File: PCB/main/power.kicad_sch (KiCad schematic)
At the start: 0 parts

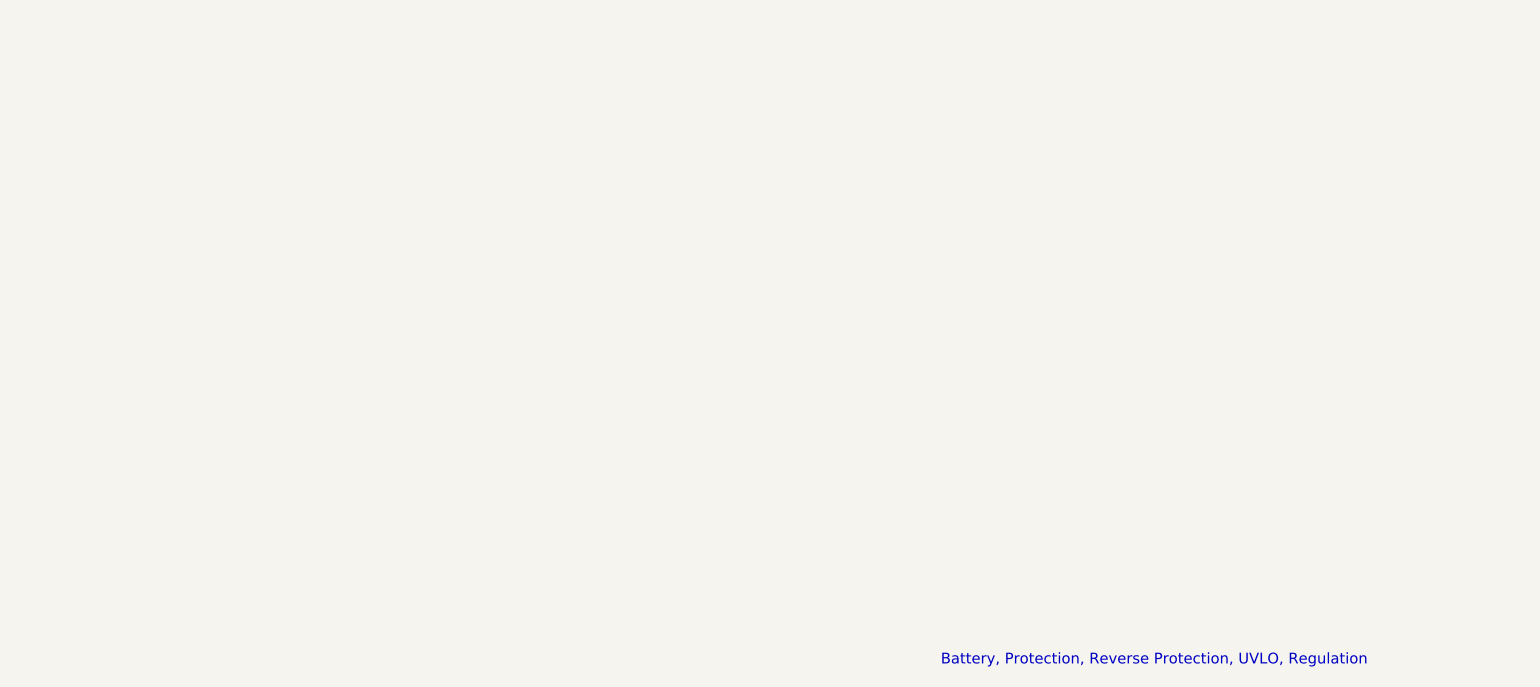
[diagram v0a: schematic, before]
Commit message: Added battery charger and polarity protection
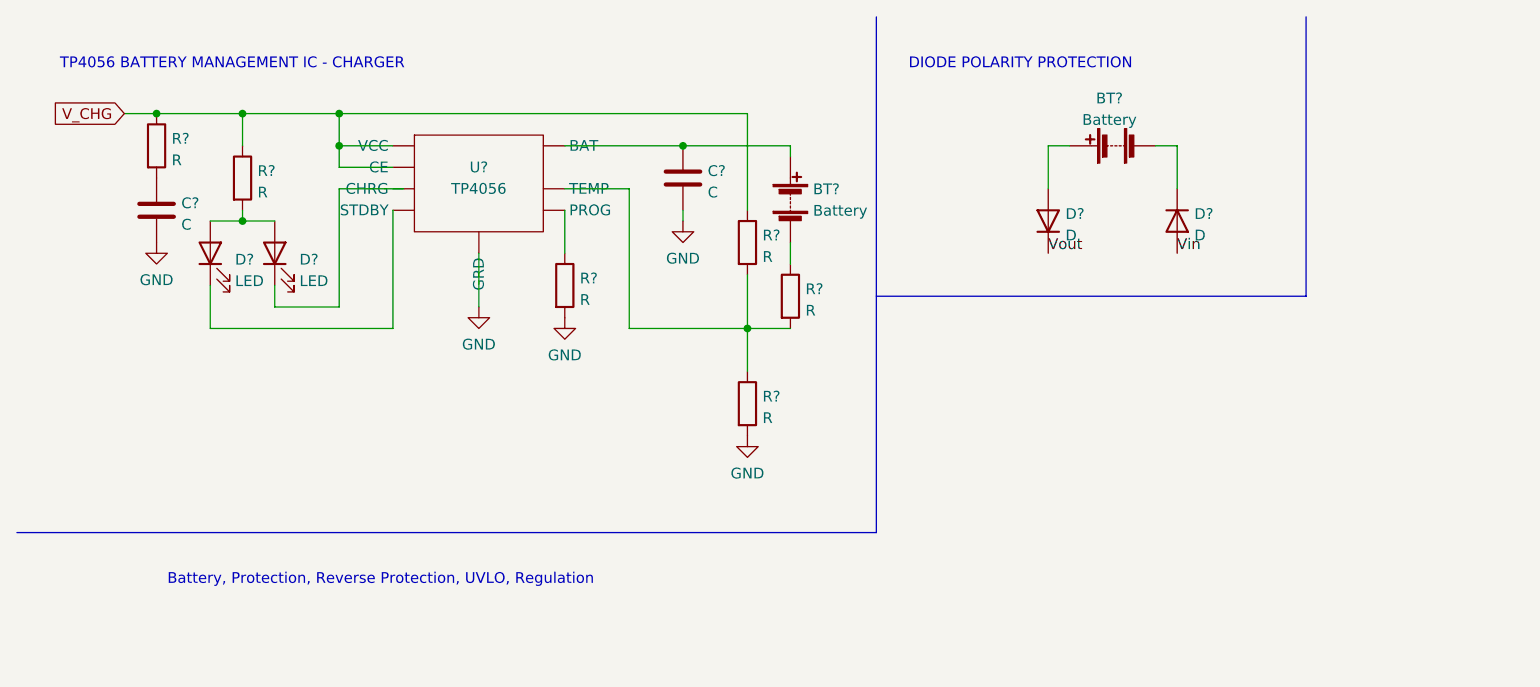
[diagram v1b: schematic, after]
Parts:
- added BT? (x2): Battery, symbol Device:Battery
- added C? (x2): C, symbol Device:C
- added D? (x2): D, symbol Device:D
- added D? (x2): LED, symbol Device:LED
- added R? (x6): R, symbol Device:R
- added U?: TP4056, symbol 000_MY_SYMBOLS:TP4056
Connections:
- new net: BT?.1 (+), C?.1
- new net: BT?.2 (-), R?.1
- new net: BT?.1 (+), D?.2 (A)
- new net: D?.2 (A), D?.2 (A), R?.2
- new net: BT?.2 (-), D?.1 (K)
- new net: C?.1, R?.2
- new net: R?.1, R?.2, R?.2
- new net GND: C?.2, C?.2, R?.2, R?.2
- new net V_CHG: R?.1, R?.1, R?.1
- new net Vin: D?.2 (A)
- new net Vout: D?.1 (K)
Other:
- note added: "DIODE POLARITY PROTECTION"
- note added: "TP4056 BATTERY MANAGEMENT IC - CHARGER"

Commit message: Added Added global V3.3 label & power BOM again again
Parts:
- removed BT?: Battery, symbol Device:Battery
- added C3: 0.47u, symbol Device:C
- added C4: 33u, symbol Device:C
- added D5: D_Zener, symbol Device:D_Zener
- added Q1: Q_PMOS_DGS, symbol Device:Q_PMOS_DGS
- added R10, R11, R12, R7, R8, R9: R, symbol Device:R
- added U2: LM3940, symbol 000_MY_SYMBOLS:LM3940
- added U3: OPAMP, symbol pspice:OPAMP
- gave numbers to parts that had none: 14
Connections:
- net GND: now also U1. (VCC), C3.2, C4.2, U2. (OUT)
- net V_CHG: now also U1. (VCC)
- net Vin: now also R10.2, R8.2, U3.5 (V-)
- net Vout: now also Q1.3 (S), R7.1, R9.1, U3.4 (V+)
- net CHG+: now reaches C2.1
- net CHG+: now also BT1.1 (+), D3.2 (A), U1. (VCC)
- net CHG-: now reaches R6.1
- net CHG-: now also BT1.2 (-), D4.1 (K)
- net at D1.1 (K): now also U1. (VCC)
- net at D2.1 (K): now also U1. (VCC)
- net at R4.2, R5.1, R6.2: now also U1. (VCC)
- net at R3.1: now also U1. (VCC)
- new net: R7.2, R8.1, U3.2 (-)
- new net: Q1.2 (G), R11.1
- new net: R11.2, R12.1, U3.3
- new net: D5.2 (A), R10.1, R12.2
- new net: D5.1 (K), R9.2, U3.1 (+)
- new net: C3.1, U2. (OUT)
- new net OUTPUT VOLTAGE: Q1.1 (D)
- new net V3.3: C4.1, U2. (OUT)
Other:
- note added: "ALL VALUES TBC"
- note added: "Cameron made this."
- note added: "UNDER VOLTAGE LOCKOUT"
- note added: "VOLTAGE REGULATOR"
- moved on the sheet: D3

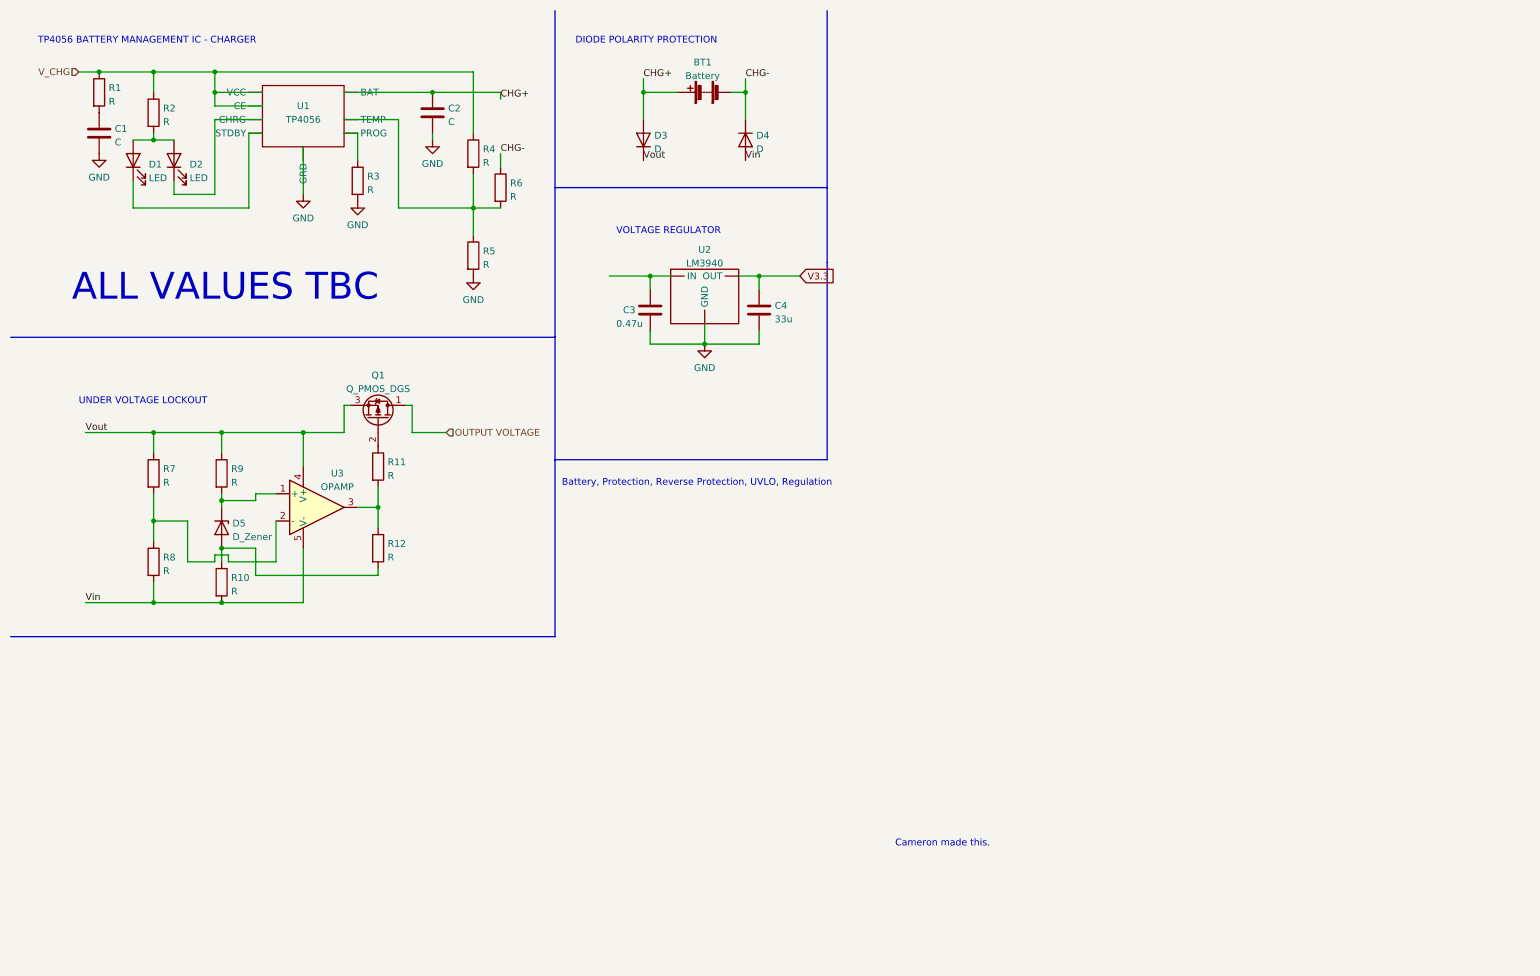
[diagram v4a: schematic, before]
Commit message: Updated power subsystem to V0.3
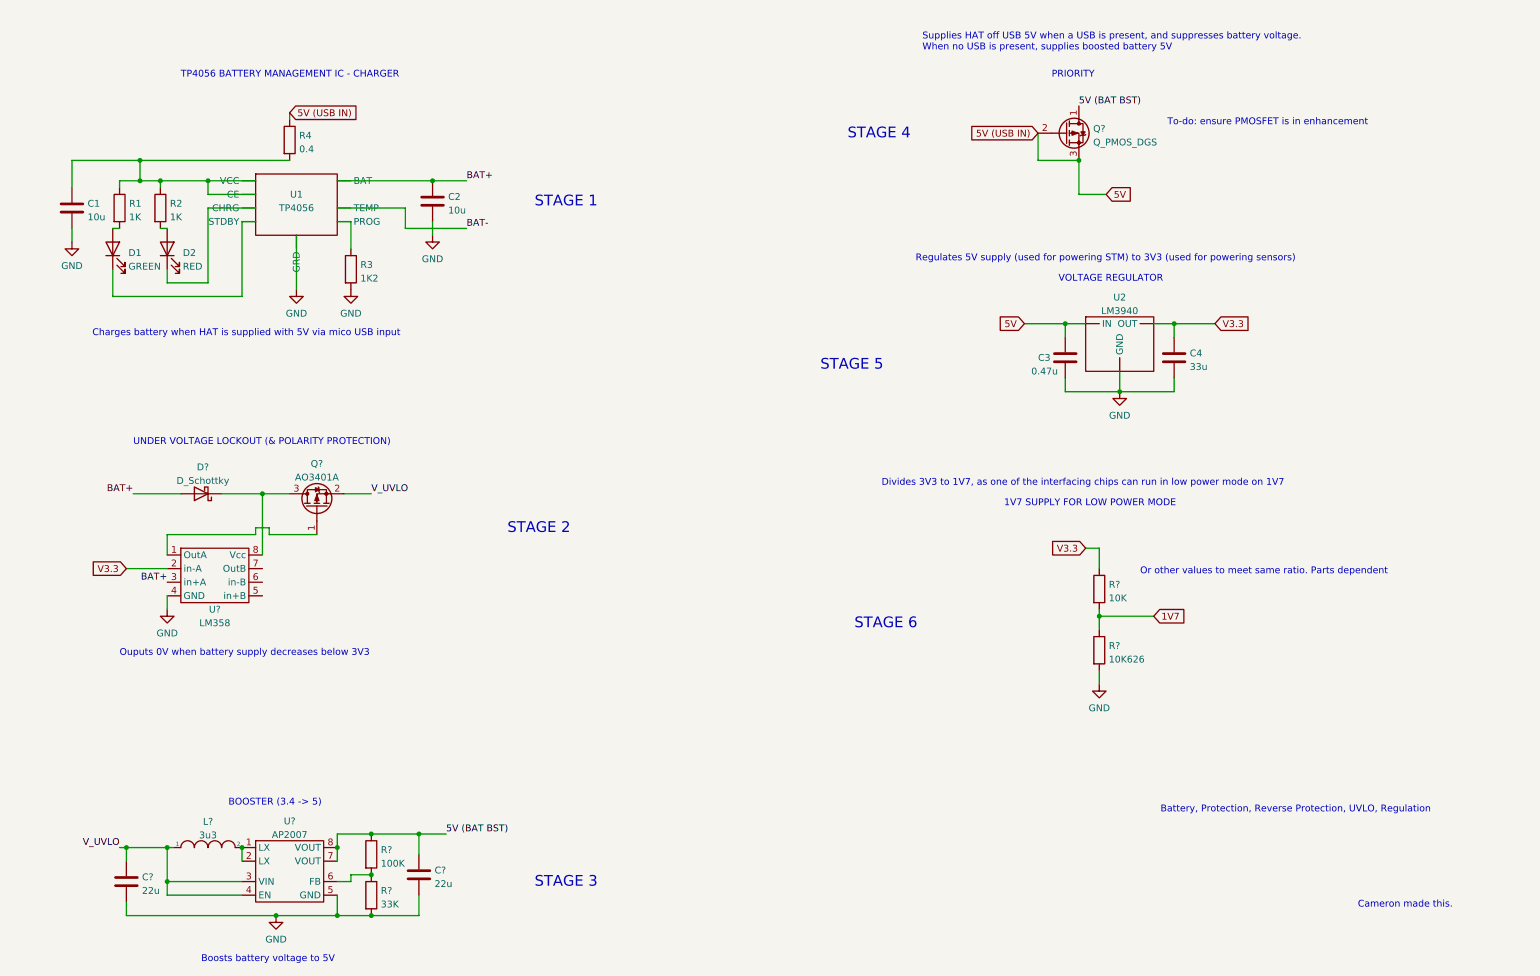
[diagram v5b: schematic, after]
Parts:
- removed BT1: Battery, symbol Device:Battery
- removed D3, D4: D, symbol Device:D
- removed D5: D_Zener, symbol Device:D_Zener
- removed Q1: Q_PMOS_DGS, symbol Device:Q_PMOS_DGS
- removed R10, R11, R12, R5, R6, R7, R8, R9: R, symbol Device:R
- removed U3: OPAMP, symbol pspice:OPAMP
- added C? (x2): 22u, symbol Device:C
- added D?: D_Schottky, symbol Device:D_Schottky
- added L?: 3u3, symbol pspice:INDUCTOR
- added Q?: Q_PMOS_DGS, symbol Device:Q_PMOS_DGS
- added Q?: AO3401A, Package_TO_SOT_SMD:SOT-23, symbol Transistor_FET:AO3401A
- added R?: 10K626, symbol Device:R
- added R?: 33K, symbol Device:R
- added R?: 10K, symbol Device:R
- added R?: 100K, symbol Device:R
- added U?: AP2007, symbol 000_MY_SYMBOLS:AP2007
- added U?: LM358, symbol 000_MY_SYMBOLS:LM358
- C1, C2: value C -> 10u
- D1: value LED -> GREEN
- D2: value LED -> RED
- R1, R2: value R -> 1K
- R3: value R -> 1K2
- R4: value R -> 0.4
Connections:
- net GND: now also C?.2, C?.2, R?.2, R?.2, U?.4 (GND), U?.5 (GND)
- net V3.3: now also R?.1, U?.2 (in-A)
- net at R4.2, U1. (VCC): now also C1.1, R1.1, R2.1
- net at D2.2 (A), R2.2: no longer D1.2 (A)
- net 5V: now reaches C3.1, U2. (OUT)
- net 5V: now also R4.1, Q?.2 (G), Q?.3 (S)
- net at R1.2: now also D1.2 (A); no longer C1.1
- net CHG+ renamed BAT+
- net BAT+: now also D?.2 (A), U?.3 (in+A)
- removed net V_CHG: R1.1, R2.1, R4.1, U1. (VCC)
- new net: Q?.1 (G), U?.1 (OutA)
- new net: D?.1 (K), Q?.3 (D), U?.8 (Vcc)
- new net: R?.1, R?.2, U?.6 (FB)
- new net: L?.2, U?.1 (LX), U?.2 (LX)
- new net 1V7: R?.1, R?.2
- new net 5V (BAT BST): C?.1, Q?.1 (D), R?.1, U?.7 (VOUT), U?.8 (VOUT)
- new net BAT-: U1. (VCC)
- new net V_UVLO: C?.1, L?.1, Q?.2 (S), U?.3 (VIN), U?.4 (EN)
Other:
- note added: "1V7 SUPPLY FOR LOW POWER MODE"
- note added: "BOOSTER (3.4 -> 5)"
- note added: "Boosts battery voltage to 5V"
- note added: "Charges battery when HAT is supplied with 5V via mico USB input"
- note added: "Divides 3V3 to 1V7, as one of the interfacing chips can run in low power mode on 1V7"
- note added: "Or other values to meet same ratio. Parts dependent"
- note added: "Ouputs 0V when battery supply decreases below 3V3"
- note added: "PRIORITY"
- note added: "Regulates 5V supply (used for powering STM) to 3V3 (used for powering sensors)"
- note added: "STAGE 1"
- note added: "STAGE 2"
- note added: "STAGE 3"
- note added: "STAGE 4"
- note added: "STAGE 5"
- note added: "STAGE 6"
- note added: "Supplies HAT off USB 5V when a USB is present, and suppresses battery voltage. When no USB is present, supplies boosted battery 5V"
- note added: "To-do: ensure PMOSFET is in enhancement"
- note added: "UNDER VOLTAGE LOCKOUT (& POLARITY PROTECTION)"
- note removed: "ALL VALUES TBC"
- note removed: "DIODE POLARITY PROTECTION"
- note removed: "UNDER VOLTAGE LOCKOUT"
- company: (none) -> UCT
- title: (none) -> Power Subsystem
- moved on the sheet: C1, C3, C4, D1, D2, R3, U1, U2

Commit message: Added references to components
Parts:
- gave numbers to parts that had none: 12
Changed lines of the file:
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@@
   (symbol (lib_id "Device:Q_PMOS_DGS") (at 209.55 35.56 0) (unit 1)
     (in_bom yes) (on_board yes) (fields_autoplaced)
-    (property "Reference" "Q?" (id 0) (at 214.757 34.7253 0)
+    (property "Reference" "Q2" (id 0) (at 214.757 34.7253 0)
       (effects (font (size 1.27 1.27)) (justify left))
     )
@@
   (symbol (lib_id "Transistor_FET:AO3401A") (at 69.85 105.41 90) (unit 1)
     (in_bom yes) (on_board yes) (fields_autoplaced)
-    (property "Reference" "Q?" (id 0) (at 69.85 97.2652 90))
+    (property "Reference" "Q1" (id 0) (at 69.85 97.2652 90))
     (property "Value" "AO3401A" (id 1) (at 69.85 99.8021 90))
     (property "Footprint" "Package_TO_SOT_SMD:SOT-23" (id 2) (at 71.755 100.33 0)
@@
   (symbol (lib_id "Device:R") (at 215.9 132.08 0) (unit 1)
     (in_bom yes) (on_board yes) (fields_autoplaced)
-    (property "Reference" "R?" (id 0) (at 217.678 131.2453 0)
+    (property "Reference" "R8" (id 0) (at 217.678 131.2453 0)
       (effects (font (size 1.27 1.27)) (justify left))
     )
@@
   (symbol (lib_id "power:GND") (at 215.9 138.43 0) (unit 1)
     (in_bom yes) (on_board yes) (fields_autoplaced)
-    (property "Reference" "#PWR?" (id 0) (at 215.9 144.78 0)
+    (property "Reference" "#PWR023" (id 0) (at 215.9 144.78 0)
       (effects (font (size 1.27 1.27)) hide)
     )
@@
   (symbol (lib_id "power:GND") (at 62.23 181.61 0) (unit 1)
     (in_bom yes) (on_board yes) (fields_autoplaced)
-    (property "Reference" "#PWR?" (id 0) (at 62.23 187.96 0)
+    (property "Reference" "#PWR022" (id 0) (at 62.23 187.96 0)
       (effects (font (size 1.27 1.27)) hide)
     )
@@
   (symbol (lib_id "Device:D_Schottky") (at 48.26 102.87 180) (unit 1)
     (in_bom yes) (on_board yes) (fields_autoplaced)
-    (property "Reference" "D?" (id 0) (at 48.5775 97.9002 0))
+    (property "Reference" "D3" (id 0) (at 48.5775 97.9002 0))
     (property "Value" "D_Schottky" (id 1) (at 48.5775 100.4371 0))
     (property "Footprint" "" (id 2) (at 48.26 102.87 0)
@@
   (symbol (lib_id "Device:R") (at 80.01 177.8 0) (unit 1)
     (in_bom yes) (on_board yes) (fields_autoplaced)
-    (property "Reference" "R?" (id 0) (at 81.788 176.9653 0)
+    (property "Reference" "R6" (id 0) (at 81.788 176.9653 0)
       (effects (font (size 1.27 1.27)) (justify left))
     )
@@
   (symbol (lib_id "000_MY_SYMBOLS:AP2007") (at 64.77 172.72 0) (unit 1)
     (in_bom yes) (on_board yes) (fields_autoplaced)
-    (property "Reference" "U?" (id 0) (at 64.77 163.991 0))
+    (property "Reference" "U8" (id 0) (at 64.77 163.991 0))
     (property "Value" "AP2007" (id 1) (at 64.77 166.5279 0))
     (property "Footprint" "" (id 2) (at 66.04 172.72 0)
@@
   (symbol (lib_id "000_MY_SYMBOLS:LM358") (at 50.8 116.84 0) (unit 1)
     (in_bom yes) (on_board yes)
-    (property "Reference" "U?" (id 0) (at 50.8 124.46 0))
+    (property "Reference" "U3" (id 0) (at 50.8 124.46 0))
     (property "Value" "LM358" (id 1) (at 50.8 127 0))
     (property "Footprint" "" (id 2) (at 50.8 116.84 0)
@@
   (symbol (lib_id "pspice:INDUCTOR") (at 49.53 168.91 0) (unit 1)
     (in_bom yes) (on_board yes) (fields_autoplaced)
-    (property "Reference" "L?" (id 0) (at 49.53 164.0672 0))
+    (property "Reference" "L1" (id 0) (at 49.53 164.0672 0))
     (property "Value" "3u3" (id 1) (at 49.53 166.6041 0))
     (property "Footprint" "" (id 2) (at 49.53 168.91 0)
@@
   (symbol (lib_id "power:GND") (at 41.91 124.46 0) (unit 1)
     (in_bom yes) (on_board yes) (fields_autoplaced)
-    (property "Reference" "#PWR?" (id 0) (at 41.91 130.81 0)
+    (property "Reference" "#PWR021" (id 0) (at 41.91 130.81 0)
       (effects (font (size 1.27 1.27)) hide)
     )
@@
   (symbol (lib_id "Device:C") (at 88.9 173.99 0) (unit 1)
     (in_bom yes) (on_board yes) (fields_autoplaced)
-    (property "Reference" "C?" (id 0) (at 91.821 173.1553 0)
+    (property "Reference" "C11" (id 0) (at 91.821 173.1553 0)
       (effects (font (size 1.27 1.27)) (justify left))
     )
@@
   (symbol (lib_id "Device:R") (at 215.9 120.65 0) (unit 1)
     (in_bom yes) (on_board yes) (fields_autoplaced)
-    (property "Reference" "R?" (id 0) (at 217.678 119.8153 0)
+    (property "Reference" "R7" (id 0) (at 217.678 119.8153 0)
       (effects (font (size 1.27 1.27)) (justify left))
     )
@@
   (symbol (lib_id "Device:R") (at 80.01 170.18 0) (unit 1)
     (in_bom yes) (on_board yes) (fields_autoplaced)
-    (property "Reference" "R?" (id 0) (at 81.788 169.3453 0)
+    (property "Reference" "R5" (id 0) (at 81.788 169.3453 0)
       (effects (font (size 1.27 1.27)) (justify left))
     )
@@
   (symbol (lib_id "Device:C") (at 34.29 175.26 0) (unit 1)
     (in_bom yes) (on_board yes) (fields_autoplaced)
-    (property "Reference" "C?" (id 0) (at 37.211 174.4253 0)
-      (effects (font (size 1.27 1.27)) (justify left))
-    )
+    (property "Reference" "C10" (id 0) (at 37.211 174.4253 0)
+      (effects (font (size 1.27 1.27)) (justify left))
+    )
